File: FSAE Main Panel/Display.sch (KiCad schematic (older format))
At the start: 66 parts, among them U501 TLC6C598, U502 TLC6C5816, U503 TLC6C5816, U504 TLC6C5816

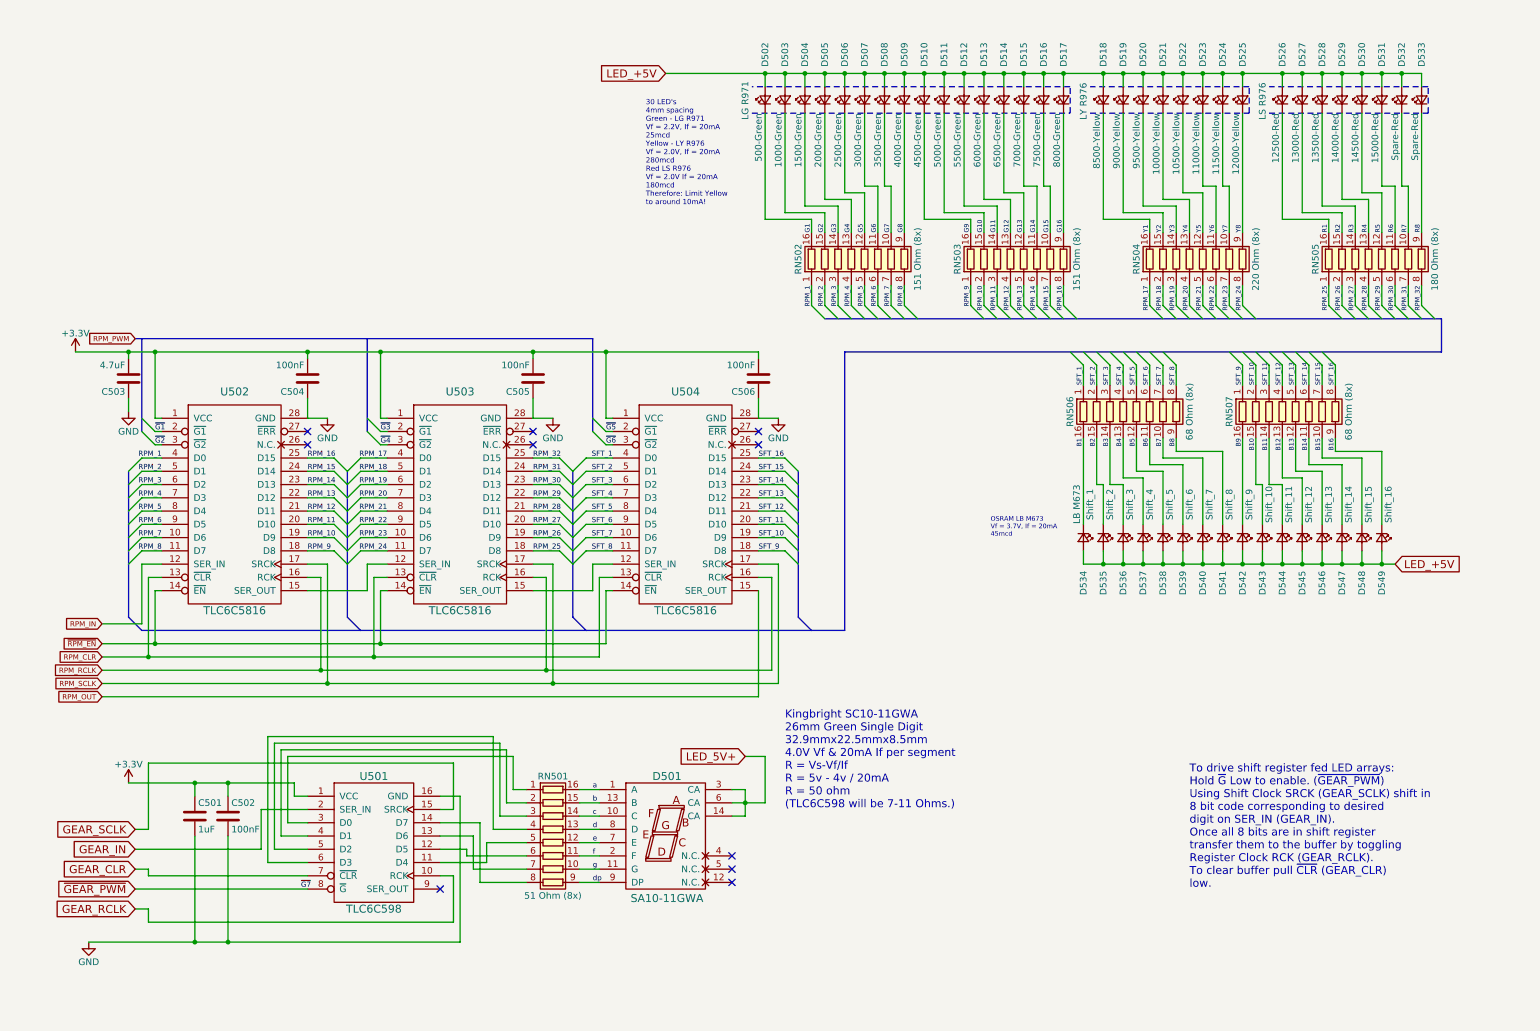
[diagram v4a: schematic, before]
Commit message: Added Warning Lights
Added Warning lights and started bulk routing
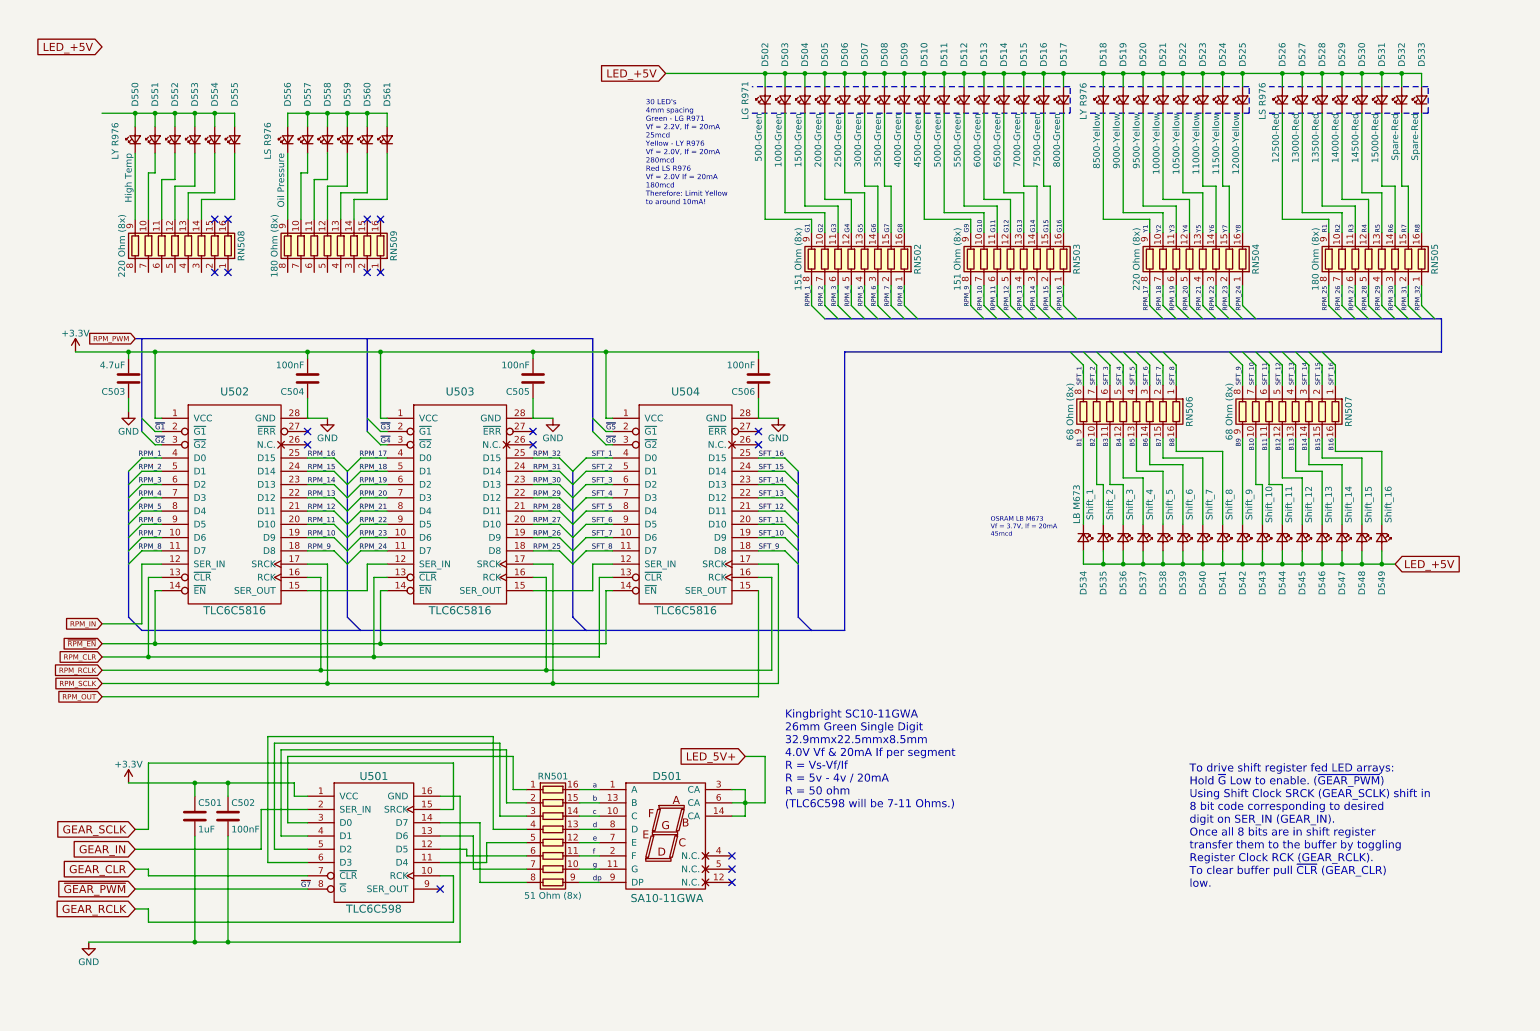
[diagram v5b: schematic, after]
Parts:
- added D550, D551, D552, D553, D554, D555: LY R976, LEDs:LED_0805, symbol Device:LED_Small
- added D556, D557, D558, D559, D560, D561: LS R976, LEDs:LED_0805, symbol Device:LED_Small
- added RN508: 220 Ohm (8x), Bourns 4800P:Bourns 4800P SOM-16, symbol Device:R_Pack08
- added RN509: 180 Ohm (8x), Bourns 4800P:Bourns 4800P SOM-16, symbol Device:R_Pack08
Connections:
- net B1: now also RN506.9 (R8.2); no longer RN506.16 (R1.2)
- net B10: now also RN507.10 (R7.2); no longer RN507.15 (R2.2)
- net B11: now also RN507.11 (R6.2); no longer RN507.14 (R3.2)
- net B12: now also RN507.12 (R5.2); no longer RN507.13 (R4.2)
- net B13: now also RN507.13 (R4.2); no longer RN507.12 (R5.2)
- net B14: now also RN507.14 (R3.2); no longer RN507.11 (R6.2)
- net B15: now also RN507.15 (R2.2); no longer RN507.10 (R7.2)
- net B16: now also RN507.16 (R1.2); no longer RN507.9 (R8.2)
- net B2: now also RN506.10 (R7.2); no longer RN506.15 (R2.2)
- net B3: now also RN506.11 (R6.2); no longer RN506.14 (R3.2)
- net B4: now also RN506.12 (R5.2); no longer RN506.13 (R4.2)
- net B5: now also RN506.13 (R4.2); no longer RN506.12 (R5.2)
- net B6: now also RN506.14 (R3.2); no longer RN506.11 (R6.2)
- net B7: now also RN506.15 (R2.2); no longer RN506.10 (R7.2)
- net B8: now also RN506.16 (R1.2); no longer RN506.9 (R8.2)
- net B9: now also RN507.9 (R8.2); no longer RN507.16 (R1.2)
- net G1: now also RN502.9 (R8.2); no longer RN502.16 (R1.2)
- net G10: now also RN503.10 (R7.2); no longer RN503.15 (R2.2)
- net G11: now also RN503.11 (R6.2); no longer RN503.14 (R3.2)
- net G12: now also RN503.12 (R5.2); no longer RN503.13 (R4.2)
- net G13: now also RN503.13 (R4.2); no longer RN503.12 (R5.2)
- net G14: now also RN503.14 (R3.2); no longer RN503.11 (R6.2)
- net G15: now also RN503.15 (R2.2); no longer RN503.10 (R7.2)
- net G16: now also RN503.16 (R1.2); no longer RN503.9 (R8.2)
- net G2: now also RN502.10 (R7.2); no longer RN502.15 (R2.2)
- net G3: now also RN502.11 (R6.2); no longer RN502.14 (R3.2)
- net G4: now also RN502.12 (R5.2); no longer RN502.13 (R4.2)
- net G5: now also RN502.13 (R4.2); no longer RN502.12 (R5.2)
- net G6: now also RN502.14 (R3.2); no longer RN502.11 (R6.2)
- net G7: now also RN502.15 (R2.2); no longer RN502.10 (R7.2)
- net G8: now also RN502.16 (R1.2); no longer RN502.9 (R8.2)
- net G9: now also RN503.9 (R8.2); no longer RN503.16 (R1.2)
- net R1: now also RN505.9 (R8.2); no longer RN505.16 (R1.2)
- net R2: now also RN505.10 (R7.2); no longer RN505.15 (R2.2)
- net R3: now also RN505.11 (R6.2); no longer RN505.14 (R3.2)
- net R4: now also RN505.12 (R5.2); no longer RN505.13 (R4.2)
- net R5: now also RN505.13 (R4.2); no longer RN505.12 (R5.2)
- net R6: now also RN505.14 (R3.2); no longer RN505.11 (R6.2)
- net R7: now also RN505.15 (R2.2); no longer RN505.10 (R7.2)
- net R8: now also RN505.16 (R1.2); no longer RN505.9 (R8.2)
- net RPM_1: now also RN502.8 (R8.1); no longer RN502.1 (R1.1)
- net RPM_10: now also RN503.7 (R7.1); no longer RN503.2 (R2.1)
- net RPM_11: now also RN503.6 (R6.1); no longer RN503.3 (R3.1)
- net RPM_12: now also RN503.5 (R5.1); no longer RN503.4 (R4.1)
- net RPM_13: now also RN503.4 (R4.1); no longer RN503.5 (R5.1)
- net RPM_14: now also RN503.3 (R3.1); no longer RN503.6 (R6.1)
- net RPM_15: now also RN503.2 (R2.1); no longer RN503.7 (R7.1)
- net RPM_16: now also RN503.1 (R1.1); no longer RN503.8 (R8.1)
- net RPM_17: now also RN504.8 (R8.1); no longer RN504.1 (R1.1)
- net RPM_18: now also RN504.7 (R7.1); no longer RN504.2 (R2.1)
- net RPM_19: now also RN504.6 (R6.1); no longer RN504.3 (R3.1)
- net RPM_2: now also RN502.7 (R7.1); no longer RN502.2 (R2.1)
- net RPM_20: now also RN504.5 (R5.1); no longer RN504.4 (R4.1)
- net RPM_21: now also RN504.4 (R4.1); no longer RN504.5 (R5.1)
- net RPM_22: now also RN504.3 (R3.1); no longer RN504.6 (R6.1)
- net RPM_23: now also RN504.2 (R2.1); no longer RN504.7 (R7.1)
- net RPM_24: now also RN504.1 (R1.1); no longer RN504.8 (R8.1)
- net RPM_25: now also RN505.8 (R8.1); no longer RN505.1 (R1.1)
- net RPM_26: now also RN505.7 (R7.1); no longer RN505.2 (R2.1)
- net RPM_27: now also RN505.6 (R6.1); no longer RN505.3 (R3.1)
- net RPM_28: now also RN505.5 (R5.1); no longer RN505.4 (R4.1)
- net RPM_29: now also RN505.4 (R4.1); no longer RN505.5 (R5.1)
- net RPM_3: now also RN502.6 (R6.1); no longer RN502.3 (R3.1)
- net RPM_30: now also RN505.3 (R3.1); no longer RN505.6 (R6.1)
- net RPM_31: now also RN505.2 (R2.1); no longer RN505.7 (R7.1)
- net RPM_32: now also RN505.1 (R1.1); no longer RN505.8 (R8.1)
- net RPM_4: now also RN502.5 (R5.1); no longer RN502.4 (R4.1)
- net RPM_5: now also RN502.4 (R4.1); no longer RN502.5 (R5.1)
- net RPM_6: now also RN502.3 (R3.1); no longer RN502.6 (R6.1)
- net RPM_7: now also RN502.2 (R2.1); no longer RN502.7 (R7.1)
- net RPM_8: now also RN502.1 (R1.1); no longer RN502.8 (R8.1)
- net RPM_9: now also RN503.8 (R8.1); no longer RN503.1 (R1.1)
- net SFT_1: now also RN506.8 (R8.1); no longer RN506.1 (R1.1)
- net SFT_10: now also RN507.7 (R7.1); no longer RN507.2 (R2.1)
- net SFT_11: now also RN507.6 (R6.1); no longer RN507.3 (R3.1)
- net SFT_12: now also RN507.5 (R5.1); no longer RN507.4 (R4.1)
- net SFT_13: now also RN507.4 (R4.1); no longer RN507.5 (R5.1)
- net SFT_14: now also RN507.3 (R3.1); no longer RN507.6 (R6.1)
- net SFT_15: now also RN507.2 (R2.1); no longer RN507.7 (R7.1)
- net SFT_16: now also RN507.1 (R1.1); no longer RN507.8 (R8.1)
- net SFT_2: now also RN506.7 (R7.1); no longer RN506.2 (R2.1)
- net SFT_3: now also RN506.6 (R6.1); no longer RN506.3 (R3.1)
- net SFT_4: now also RN506.5 (R5.1); no longer RN506.4 (R4.1)
- net SFT_5: now also RN506.4 (R4.1); no longer RN506.5 (R5.1)
- net SFT_6: now also RN506.3 (R3.1); no longer RN506.6 (R6.1)
- net SFT_7: now also RN506.2 (R2.1); no longer RN506.7 (R7.1)
- net SFT_8: now also RN506.1 (R1.1); no longer RN506.8 (R8.1)
- net SFT_9: now also RN507.8 (R8.1); no longer RN507.1 (R1.1)
- net Y1: now also RN504.9 (R8.2); no longer RN504.16 (R1.2)
- net Y2: now also RN504.10 (R7.2); no longer RN504.15 (R2.2)
- net Y3: now also RN504.11 (R6.2); no longer RN504.14 (R3.2)
- net Y4: now also RN504.12 (R5.2); no longer RN504.13 (R4.2)
- net Y5: now also RN504.13 (R4.2); no longer RN504.12 (R5.2)
- net Y6: now also RN504.14 (R3.2); no longer RN504.11 (R6.2)
- net Y7: now also RN504.15 (R2.2); no longer RN504.10 (R7.2)
- net Y8: now also RN504.16 (R1.2); no longer RN504.9 (R8.2)
- new net: D550.1 (K), RN508.9 (R8.2)
- new net: D550.2 (A), D551.2 (A), D552.2 (A), D553.2 (A), D554.2 (A), D555.2 (A)
- new net: D551.1 (K), RN508.10 (R7.2)
- new net: D552.1 (K), RN508.11 (R6.2)
- new net: D553.1 (K), RN508.12 (R5.2)
- new net: D554.1 (K), RN508.13 (R4.2)
- new net: D555.1 (K), RN508.14 (R3.2)
- new net: D557.1 (K), RN509.10 (R7.2)
- new net: D558.1 (K), RN509.11 (R6.2)
- new net: D559.1 (K), RN509.12 (R5.2)
- new net: D560.1 (K), RN509.13 (R4.2)
- new net: D561.1 (K), RN509.14 (R3.2)
- new net: D556.1 (K), RN509.9 (R8.2)
- new net: D556.2 (A), D557.2 (A), D558.2 (A), D559.2 (A), D560.2 (A), D561.2 (A)
- no-connect marks 10 -> 18

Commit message: Updated PCB
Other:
- moved on the sheet: D550, D551, D552, D553, D554, D555, D556, D557, D558, D559, D560, D561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

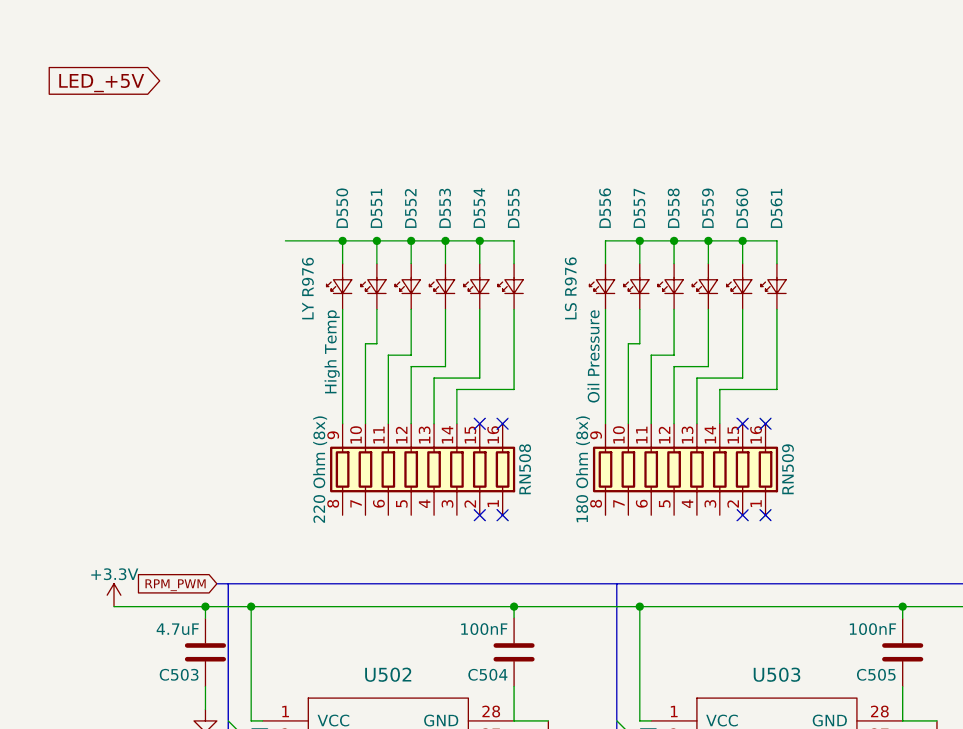
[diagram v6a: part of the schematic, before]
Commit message: Added warning nMOS circuit, simulated, updated PCB
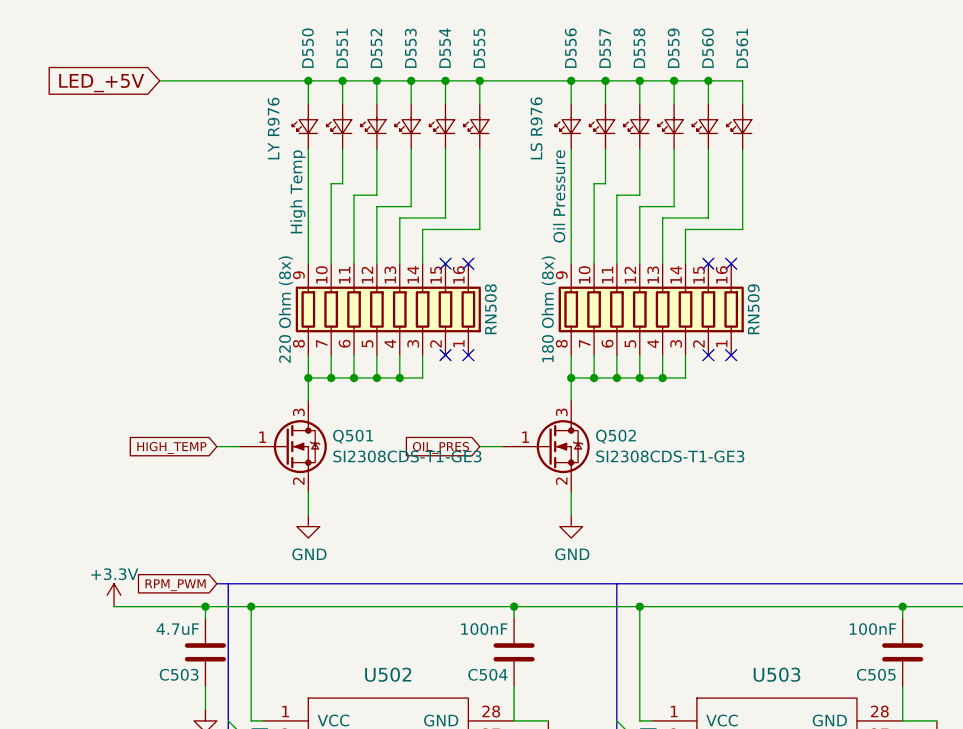
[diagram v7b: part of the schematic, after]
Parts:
- added Q501, Q502: SI2308CDS-T1-GE3, TO_SOT_Packages_SMD:SOT-23, symbol Device:Q_NMOS_GSD
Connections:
- net GND: now also Q501.2 (S), Q502.2 (S)
- net LED_+5V: now also D550.2 (A), D551.2 (A), D552.2 (A), D553.2 (A), D554.2 (A), D555.2 (A), D556.2 (A), D557.2 (A), D558.2 (A), D559.2 (A), D560.2 (A), D561.2 (A)
- net at RN508.3 (R3.1): now also RN508.4 (R4.1), RN508.5 (R5.1), RN508.6 (R6.1), RN508.7 (R7.1), RN508.8 (R8.1), Q501.3 (D)
- net at RN509.3 (R3.1): now also RN509.4 (R4.1), RN509.5 (R5.1), RN509.6 (R6.1), RN509.7 (R7.1), RN509.8 (R8.1), Q502.3 (D)
- new net HIGH_TEMP: Q501.1 (G)
- new net OIL_PRES: Q502.1 (G)
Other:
- moved on the sheet: D550, D551, D552, D553, D554, D555, D556, D557, D558, D559, D560, D561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
